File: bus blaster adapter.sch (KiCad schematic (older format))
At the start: 55 parts

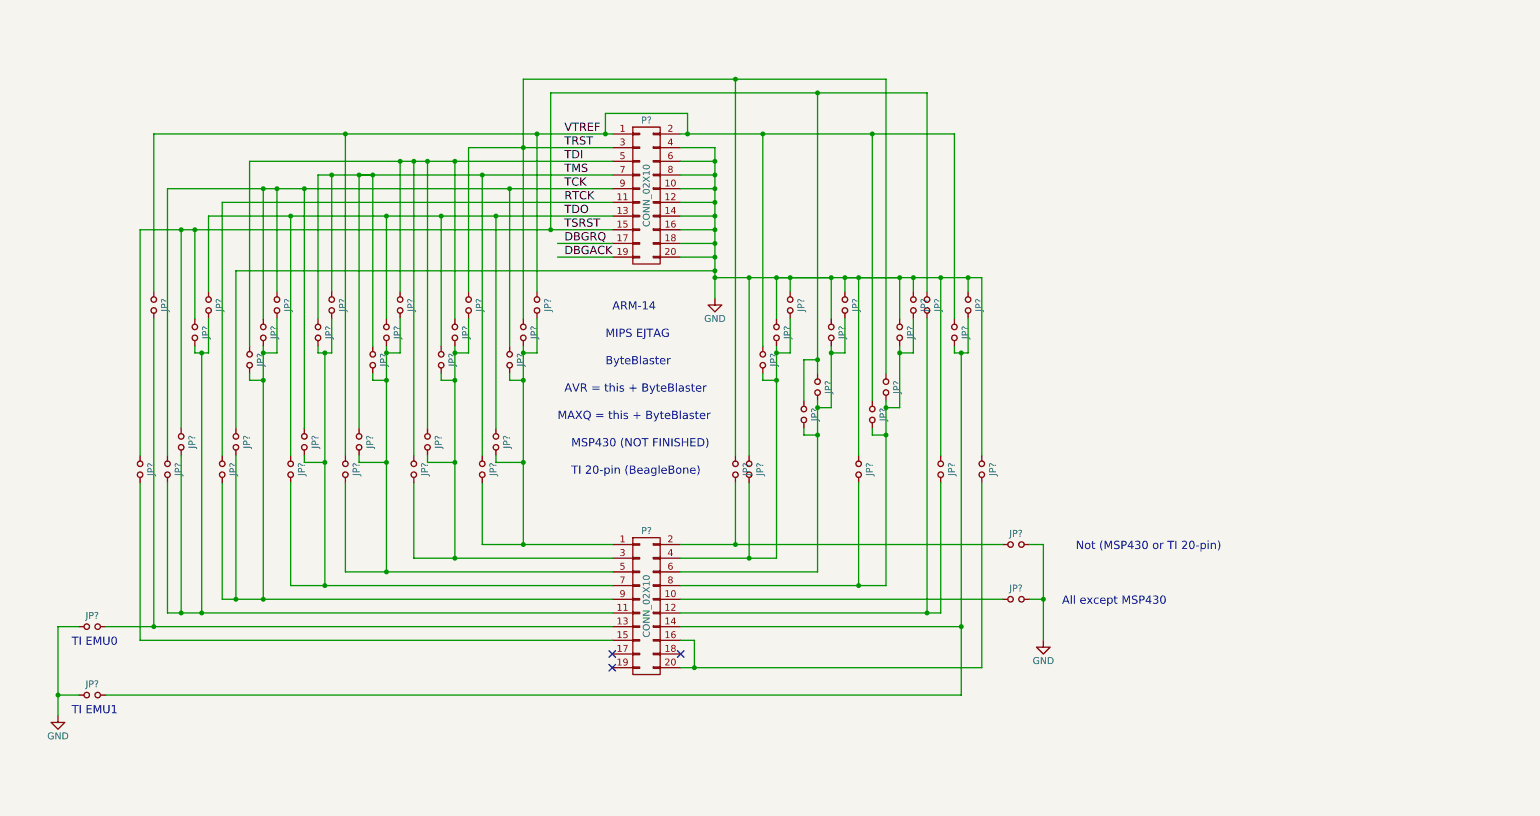
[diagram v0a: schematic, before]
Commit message: Changed half-done MSP430 to 10-pin Tag Connect
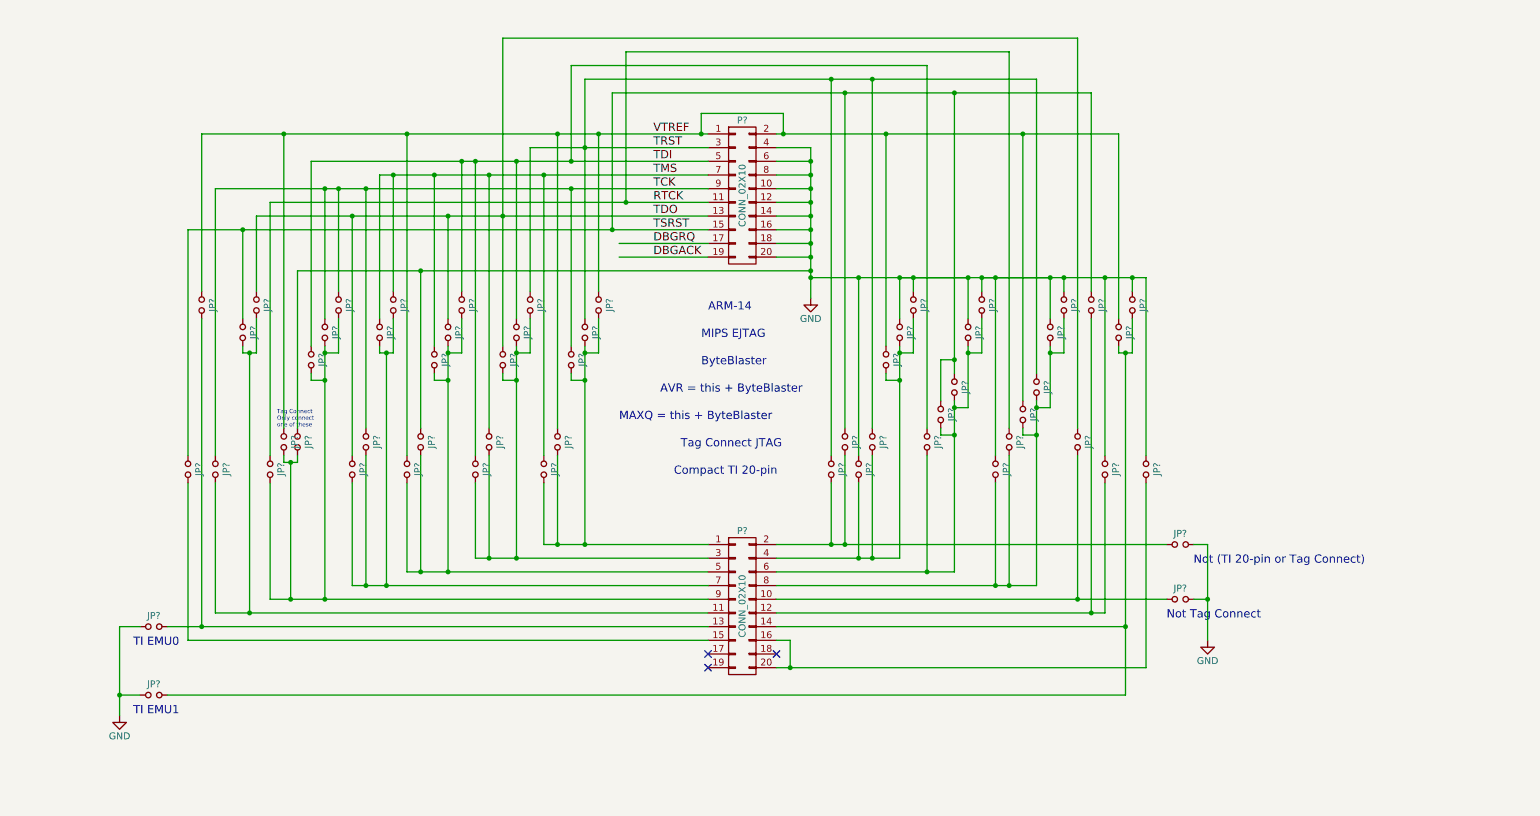
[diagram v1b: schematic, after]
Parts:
- removed JP? (x7): Jumper_NO_Small, symbol Jumper_NO_Small
- added JP? (x12): Jumper_NO_Small, symbol Jumper_NO_Small
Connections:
- net GND: now also JP?.1, JP?.1, JP?.2
- net RTCK: now also JP?.1
- net TCK: now also JP?.1
- net TDI: now also JP?.1
- net TDO: now also JP?.1
- net TMS: now also JP?.1
- net TRST: now also JP?.1
- net TSRST: now also JP?.1
- net VTREF: now also JP?.1, JP?.1
- net at JP?.2, JP?.2, JP?.2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: now also JP?.2 (x5)
- net at JP?.2, JP?.2, JP?.2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: now also JP?.2
- net at JP?.2, JP?.2, JP?.2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: now also JP?.2, JP?.2
- net at JP?.2, JP?.2, JP?.2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: now also JP?.2
- net at P?.10 (P10): now also JP?.1, JP?.2
- net at JP?.1, JP?.2, P?.2 (P2): now also JP?.2
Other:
- note added: "Compact TI 20-pin"
- note added: "Not (TI 20-pin or Tag Connect)"
- note added: "Not Tag Connect"
- note added: "Tag Connect JTAG"
- note added: "Tag Connect\nOnly connect\none of these"
- note removed: "All except MSP430"
- note removed: "MSP430 (NOT FINISHED)"
- note removed: "Not (MSP430 or TI 20-pin)"
- note removed: "TI 20-pin (BeagleBone)"
- moved on the sheet: JP?, P?

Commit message: Added Blackfin
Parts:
- added JP? (x11): Jumper_NO_Small, symbol Jumper_NO_Small
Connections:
- net GND: now also JP?.1, JP?.1, JP?.1, JP?.1, JP?.1
- net TCK: now also JP?.1
- net TDI: now also JP?.1
- net TDO: now also JP?.1
- net TMS: now also JP?.1
- net TRST: now also JP?.1
- net TSRST: now also JP?.1
- net at JP?.2, JP?.2, JP?.2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: now also JP?.2 (x2)
- net at JP?.2, JP?.2, JP?.2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: now also JP?.2 (x2)
- net at JP?.2, JP?.2, P?.13 (P13): now also JP?.2
- net at JP?.2, JP?.2, P?.12 (P12): now also JP?.2
- net at JP?.2, JP?.2, JP?.2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: now also JP?.2
- net at JP?.2, JP?.2, JP?.2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: now also JP?.2 (x2)
- net at JP?.1, JP?.2, JP?.2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: now also JP?.2
- net at JP?.1, JP?.2, P?.10 (P10): now also JP?.2
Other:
- note added: "Blackfin"
- note added: "Not (TI 20-pin or Tag Connect or Blackfin)"
- note added: "Not (Tag Connect or Blackfin)"
- note removed: "Not (TI 20-pin or Tag Connect)"
- note removed: "Not Tag Connect"
- moved on the sheet: JP?

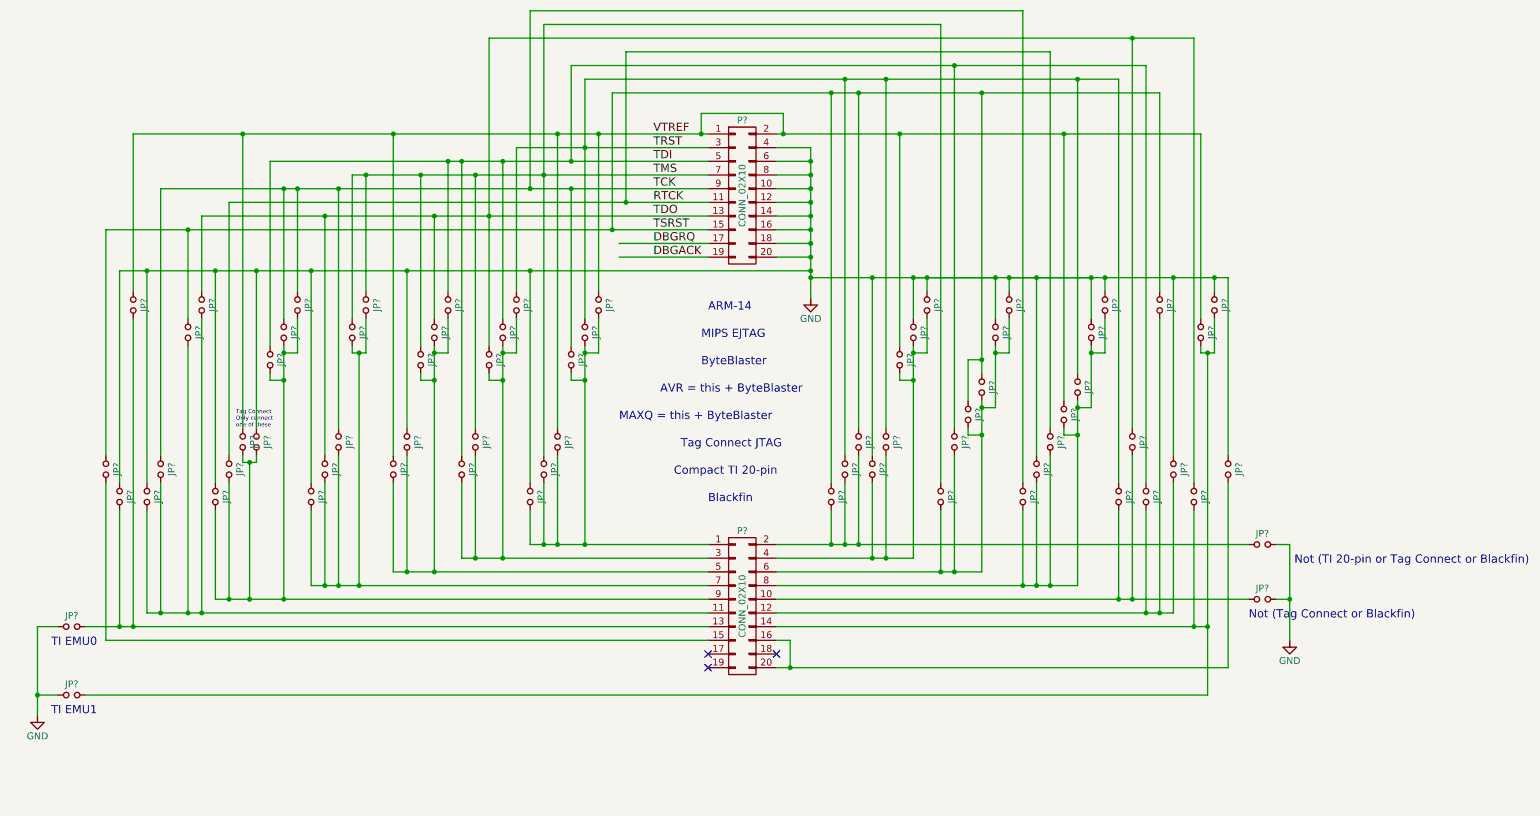
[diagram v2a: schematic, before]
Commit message: Tidy up, added VREF jumper to AVR.
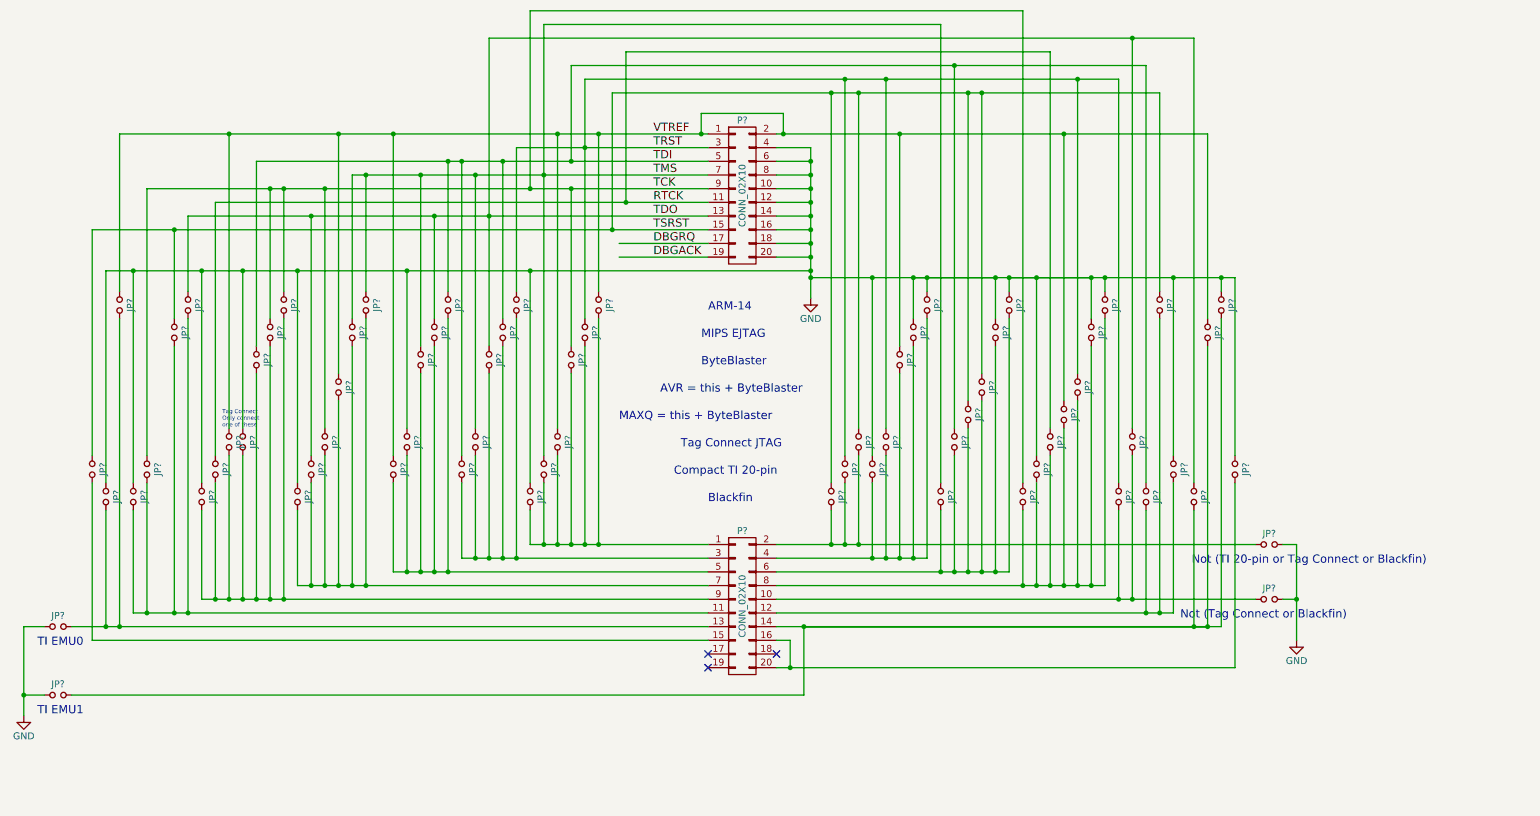
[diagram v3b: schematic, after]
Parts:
- added JP?: Jumper_NO_Small, symbol Jumper_NO_Small
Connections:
- net VTREF: now also JP?.1
- net at JP?.2, JP?.2, JP?.2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: now also JP?.2
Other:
- moved on the sheet: JP?

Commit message: Updates
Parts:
- JP101, JP102, JP103, JP104, JP105, JP106, JP107, JP108, JP109, JP110, JP111, JP112, JP113, JP114, JP115, JP116, JP117, JP118, JP119, JP120, JP121, JP122, JP123, JP124, JP125, JP126, JP127, JP128, JP129, JP130, JP131, JP132, JP133, JP134, JP135, JP136, JP137, JP138, JP139, JP140, JP141, JP142, JP143, JP144, JP145, JP146, JP147, JP148, JP149, JP150, JP151, JP152, JP153, JP154, JP155, JP156, JP157, JP158, JP159, JP160, JP161, JP162, JP163, JP164, JP165, JP166, JP167, JP168, JP169, JP170: renamed from JP?; footprint (none) -> solder jumper:0603_jumper
- P101, P102: renamed from P?; footprint (none) -> Pin_Headers:Pin_Header_Straight_2x10
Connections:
- no-connect marks 3 -> 5
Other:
- moved on the sheet: JP106, JP107, JP163, JP164

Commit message: Layout work, could probably use double checking...
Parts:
- added P103: CONN_02X05, header_1:10pin_1.27pitch, symbol CONN_02X05
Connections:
- net at JP133.2, JP134.2, JP135.2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: now also P103.1 (P1)
- net at JP128.2, JP129.2, JP130.2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: now also P103.3 (P3)
- net at JP123.2, JP124.2, JP125.2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: now also P103.5 (P5)
- net at JP117.2, JP118.2, JP119.2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: now also P103.7 (P7)
- net at JP110.2, JP111.2, JP112.2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: now also P103.9 (P9)
- net at JP153.2, JP154.2, JP155.2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: now also P103.8 (P8)
- net at JP147.2, JP148.2, JP149.2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: now also P103.6 (P6)
- net at JP142.2, JP143.2, JP144.2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: now also P103.4 (P4)
- net at JP139.2, JP140.2, JP141.2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: now also P103.2 (P2)
- net at JP160.2, JP161.2, JP170.1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: now also P103.10 (P10)
